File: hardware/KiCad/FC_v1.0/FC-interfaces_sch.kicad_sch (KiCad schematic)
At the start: 26 parts, among them J1 MEM2061-01-188-00-A, J2 USB4105-GF-A, J3 PAD_OUT, J4 FTSH-105-01-F-DV-K, U7 TPD4E05U06DQAR, U8 MCP2562FD-E/SN

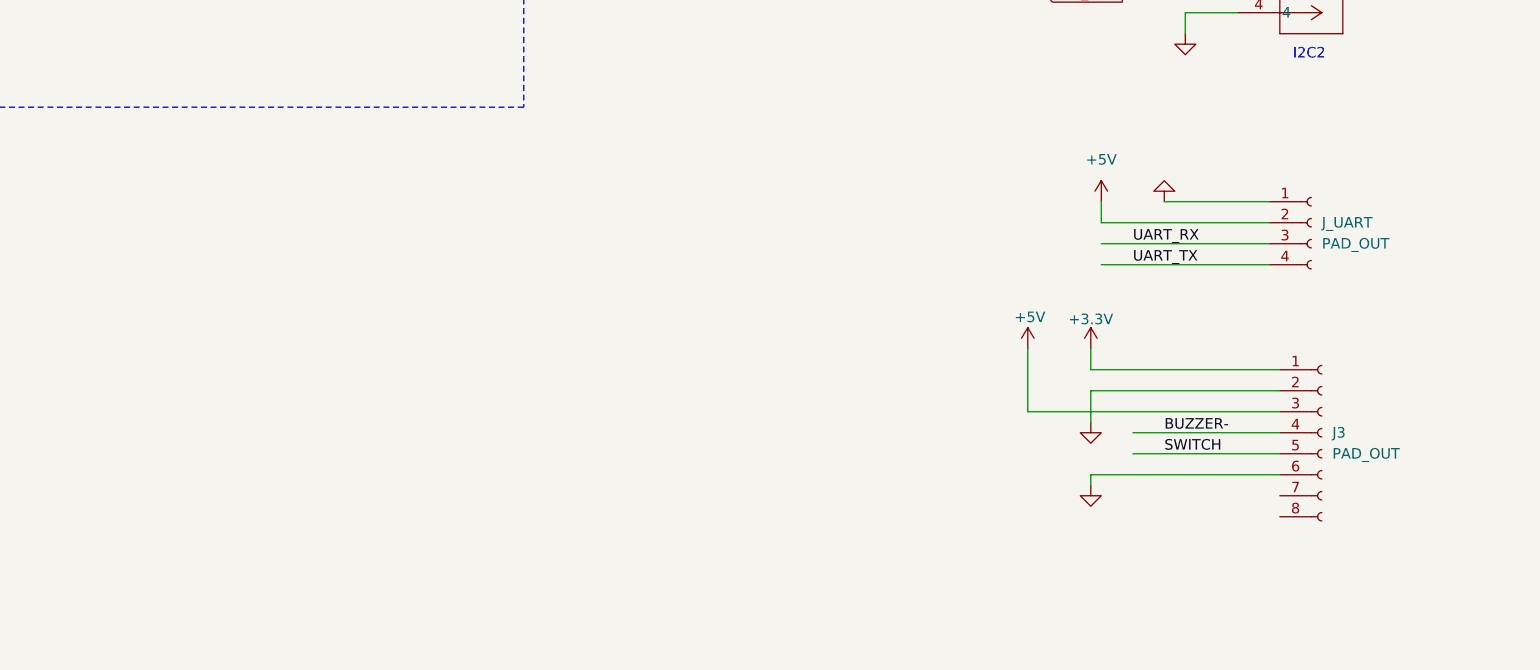
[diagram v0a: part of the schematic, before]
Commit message: Buzzer implementation
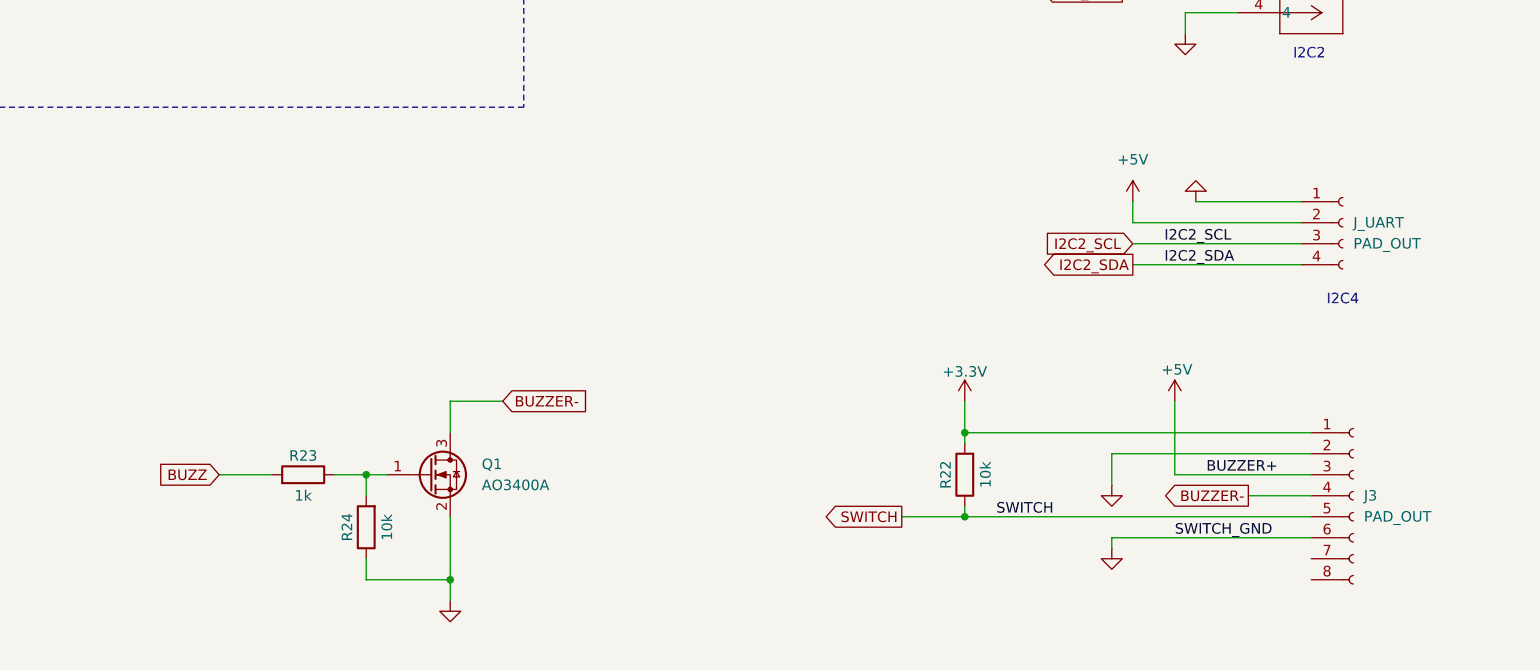
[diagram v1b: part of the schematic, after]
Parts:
- added Q1: AO3400A, Package_TO_SOT_SMD:SOT-23, symbol Transistor_FET:AO3400A
- added R22, R24: 10k, symbol Device:R
- added R23: 1k, symbol Device:R
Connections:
- net +3.3V: now also R22.2
- net BUZZER-: now also Q1.3 (D)
- net SWITCH: now also R22.1
- net SWITCH_GND: now reaches J3.6 (Pin_6)
- net UART_RX renamed I2C2_SCL
- net UART_TX renamed I2C2_SDA
- new net: Q1.1 (G), R23.1, R24.2
- new net: Q1.2 (S), R24.1
- new net BUZZ: R23.2
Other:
- note added: "I2C4"
- moved on the sheet: J3, J_UART

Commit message: ESC PWM Generation
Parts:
- added J_ESC: SM06B-GHS-TB, CONN_SM06B-GHS-TB_JST, symbol GH-6P-import:SM06B-GHS-TB
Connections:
- net +5V: now also J_ESC.1
- new net ESC_PWM1: J_ESC.2
- new net ESC_PWM2: J_ESC.3
- new net ESC_PWM3: J_ESC.4
- new net ESC_PWM4: J_ESC.5
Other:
- note added: "CAN Transceiver ------- STBY mode disabled"
- note added: "TIM1"
- note removed: "CAN Transceiver"
- note removed: "STBY mode disabled"
- moved on the sheet: J3, J_GPS, J_I2C, J_TELEM, J_UART, Q1, R22, R23, R24
